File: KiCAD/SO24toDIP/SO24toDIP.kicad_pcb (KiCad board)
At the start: 2 copper layers, 33 x 19 mm, 2 parts, among them U1 STP8DP05, U2 STP16DP05

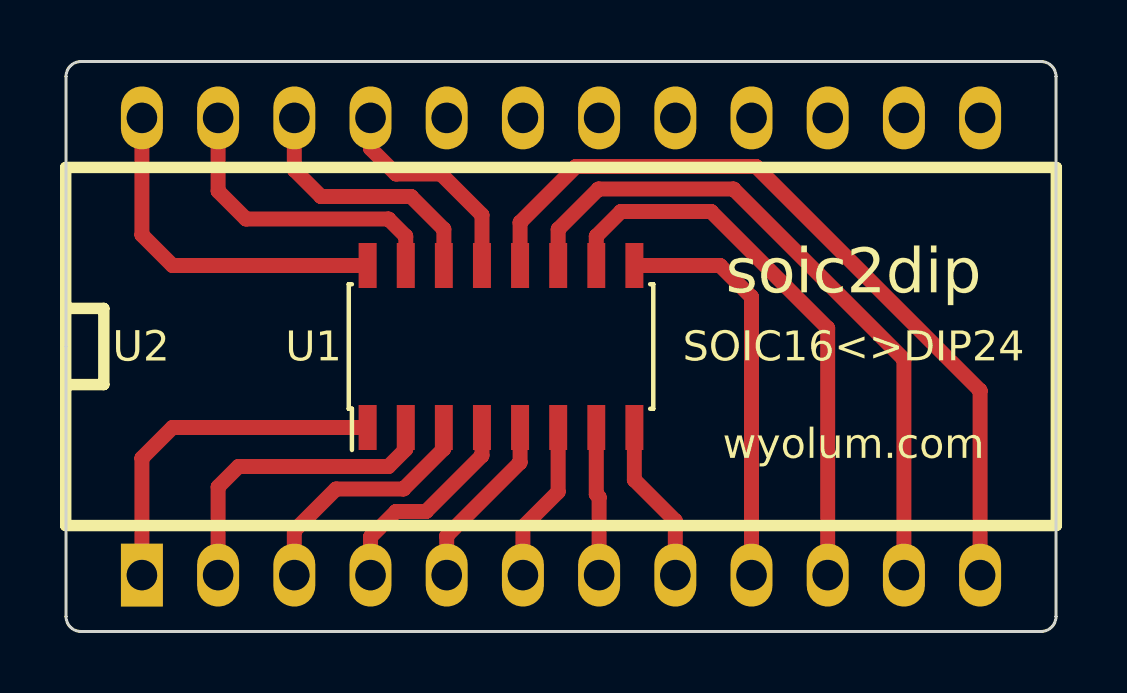
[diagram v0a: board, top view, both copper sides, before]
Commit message: added 24-SOIC to 24-DIP breakout board for 74HC154
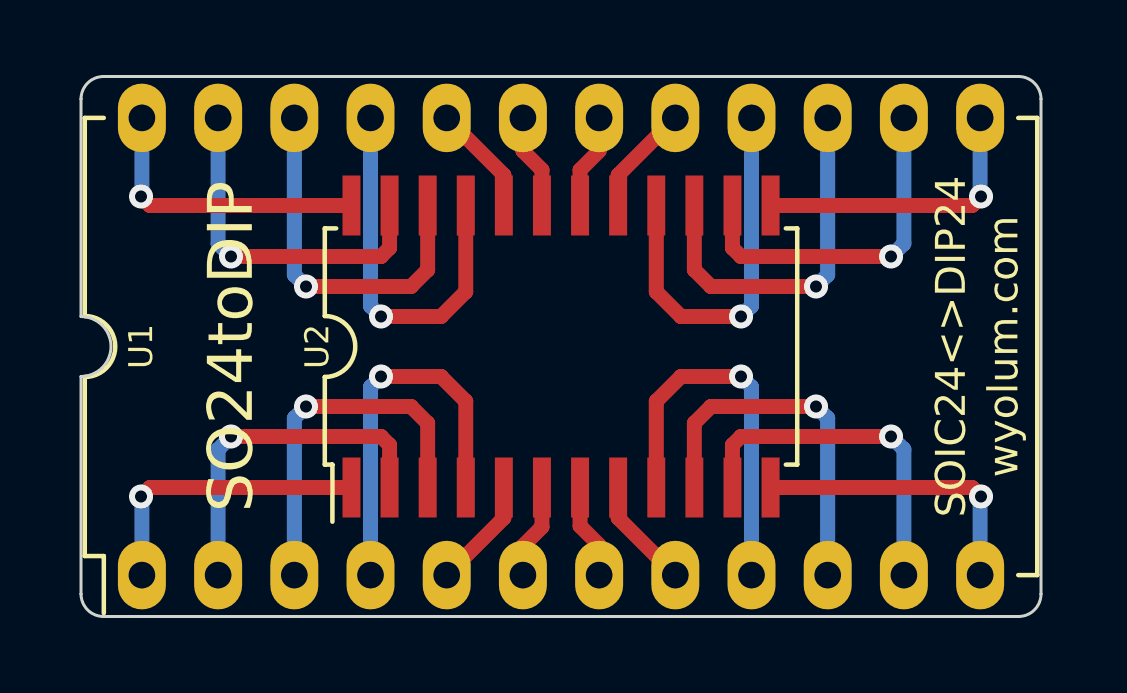
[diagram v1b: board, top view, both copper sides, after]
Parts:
- removed the U1 at (39.0, 27.0)
- added U2: 74HC154, SO24toDIP_libs:SOIC-24_7.5x15.4mm_Pitch1.27mm, F.Cu at (41.0, 27.0)
- U1: renamed from U2; value STP16DP05 -> 74HC154; footprint soic2dip_libs:DIP-24_600_ELL -> SO24toDIP_libs:DIP-24_W15.24mm_LongPads
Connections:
- U1 pad 1: /GND -> Net-(U1-Pad1)
- U1 pad 10: /OUT5 -> Net-(U1-Pad10)
- U1 pad 11: /OUT6 -> Net-(U1-Pad11)
- U1 pad 12: /OUT7 -> GND
- U1 pad 13: (no net) -> Net-(U1-Pad13)
- U1 pad 14: (no net) -> Net-(U1-Pad14)
- U1 pad 15: (no net) -> Net-(U1-Pad15)
- U1 pad 16: (no net) -> Net-(U1-Pad16)
- U1 pad 17: (no net) -> Net-(U1-Pad17)
- U1 pad 18: (no net) -> Net-(U1-Pad18)
- U1 pad 19: (no net) -> Net-(U1-Pad19)
- U1 pad 2: /SDI -> Net-(U1-Pad2)
- U1 pad 20: (no net) -> Net-(U1-Pad20)
- U1 pad 21: /OE-DM2 -> Net-(U1-Pad21)
- U1 pad 22: /SD0 -> Net-(U1-Pad22)
- U1 pad 23: /R_EXT -> Net-(U1-Pad23)
- U1 pad 24: /VCC -> VCC
- U1 pad 3: /CLK -> Net-(U1-Pad3)
- U1 pad 4: /LE-DM1 -> Net-(U1-Pad4)
- U1 pad 5: /OUT0 -> Net-(U1-Pad5)
- U1 pad 6: /OUT1 -> Net-(U1-Pad6)
- U1 pad 7: /OUT2 -> Net-(U1-Pad7)
- U1 pad 8: /OUT3 -> Net-(U1-Pad8)
- U1 pad 9: /OUT4 -> Net-(U1-Pad9)
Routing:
- net /OUT7: track 26.8 -> 0.00 mm
- net /OUT6: track 22.8 -> 0.00 mm
- net /OUT5: track 18.9 -> 0.00 mm
- net /OUT4: track 13.6 -> 0.00 mm
- net Net-(U1-Pad21): track 0.00 -> 12.8 mm, vias 0 -> 1
- net Net-(U1-Pad16): track 0.00 -> 12.8 mm, vias 0 -> 1
- net Net-(U1-Pad9): track 0.00 -> 12.8 mm, vias 0 -> 1
- net Net-(U1-Pad4): track 0.00 -> 12.8 mm, vias 0 -> 1
- net Net-(U1-Pad22): track 0.00 -> 12.2 mm, vias 0 -> 1
- net Net-(U1-Pad15): track 0.00 -> 12.2 mm, vias 0 -> 1
- net Net-(U1-Pad3): track 0.00 -> 12.2 mm, vias 0 -> 1
- net Net-(U1-Pad10): track 0.00 -> 12.2 mm, vias 0 -> 1
- net /VCC: track 11.8 -> 0.00 mm
- net /GND: track 11.8 -> 0.00 mm
- net Net-(U1-Pad23): track 0.00 -> 11.6 mm, vias 0 -> 1
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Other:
- board size 33 x 19 mm -> 32 x 18 mm
- net class 0.50: via_dia 0.6 -> 0.8
- net class Default: via_dia 0.6 -> 0.8
- board text added: "SO24toDIP"
- board text added: "SOIC24<>DIP24"
- board text removed: "SOIC16<>DIP24"
- board text removed: "soic2dip"
